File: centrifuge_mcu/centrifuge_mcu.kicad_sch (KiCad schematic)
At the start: 8 parts

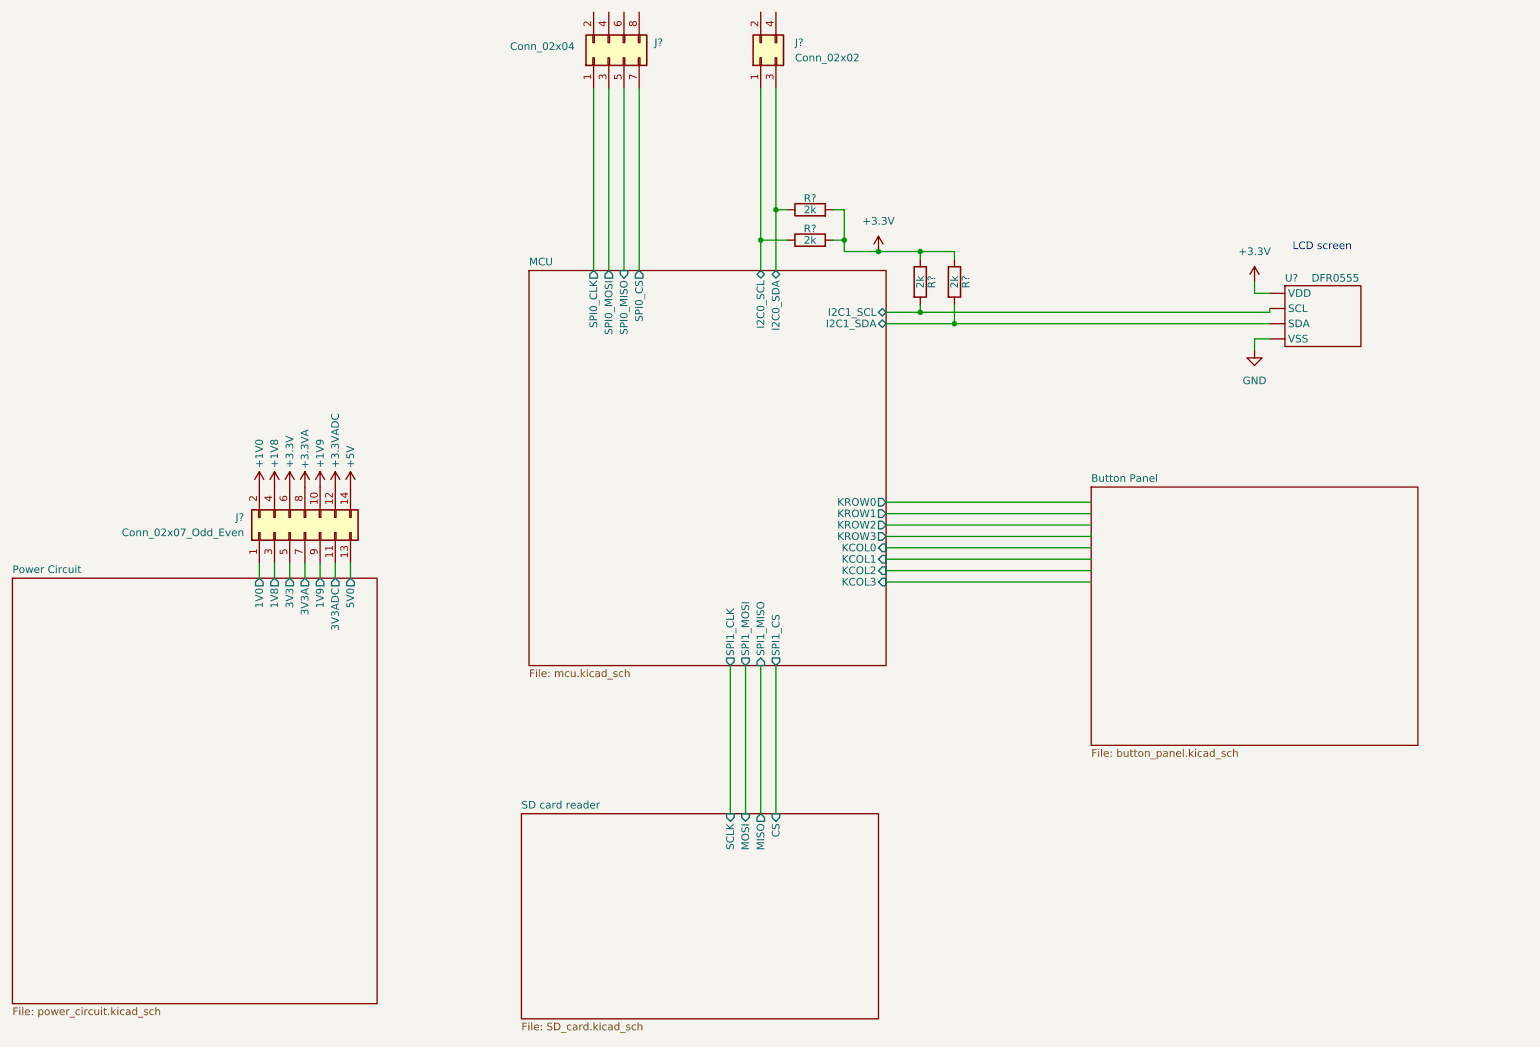
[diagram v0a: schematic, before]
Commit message: make and pick footprints for almost everything
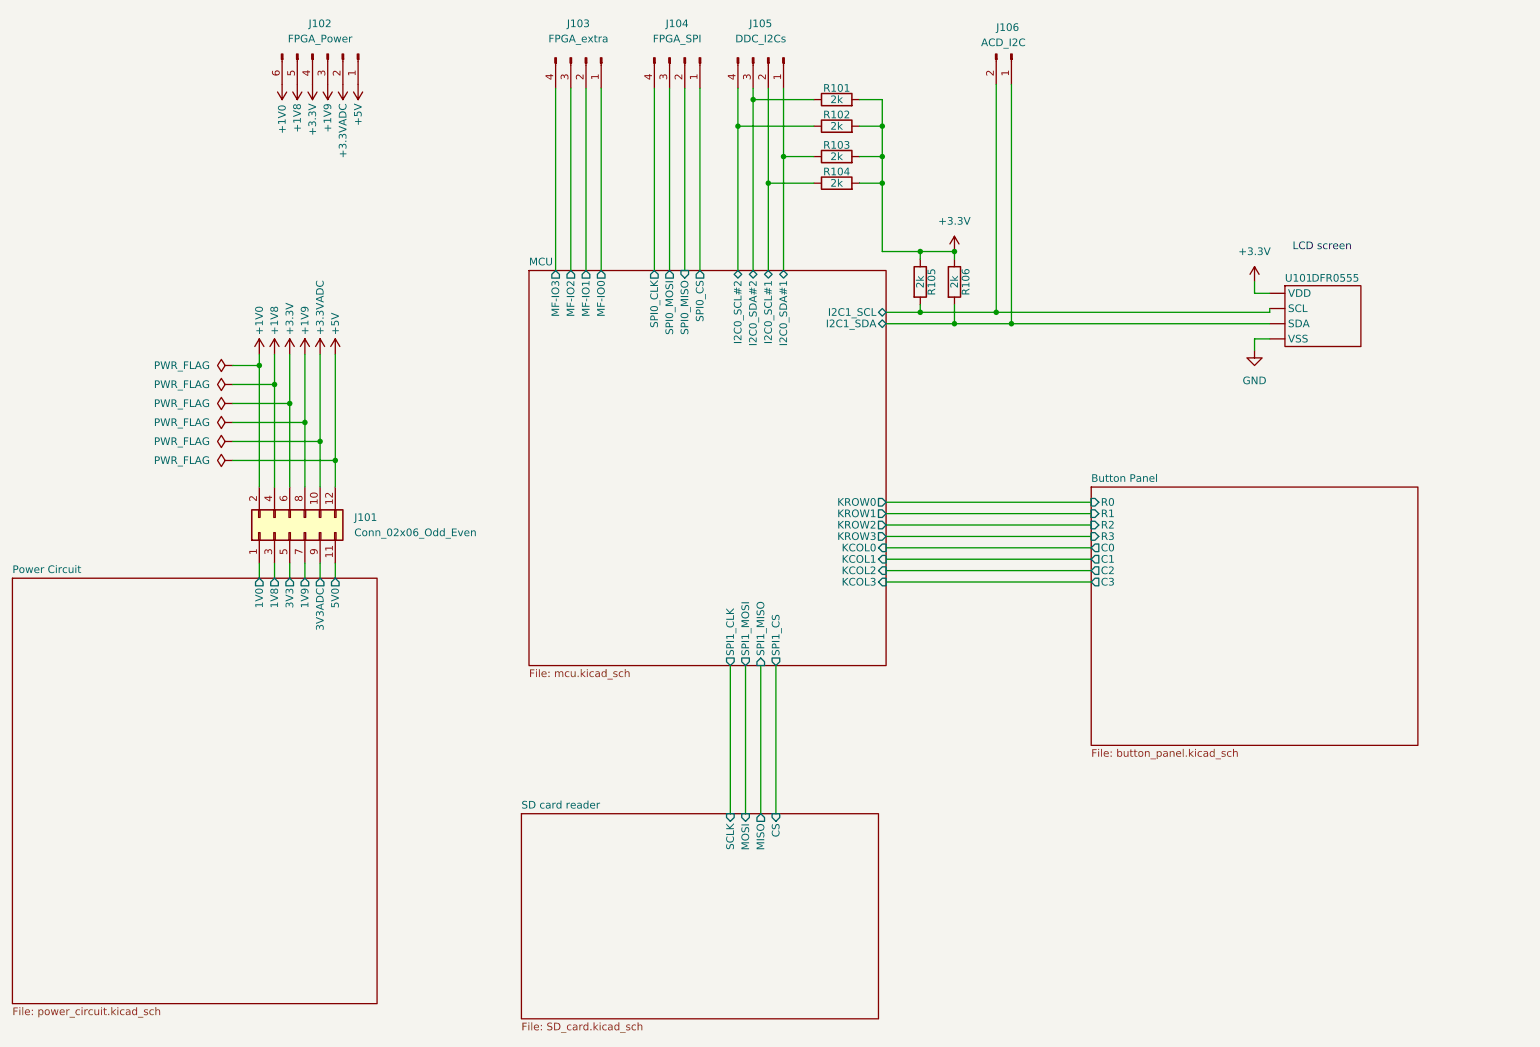
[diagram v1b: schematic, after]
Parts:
- removed J?: Conn_02x02, symbol Connector_Generic:Conn_02x02_Odd_Even
- removed J?: Conn_02x07_Odd_Even, symbol Connector_Generic:Conn_02x07_Odd_Even
- removed J?: Conn_02x04, symbol Connector_Generic:Conn_02x04_Odd_Even
- removed R? (x2): 2k, symbol Device:R
- added J101: Conn_02x06_Odd_Even, Connector_PinHeader_2.54mm:PinHeader_2x06_P2.54mm_Vertical, symbol Connector_Generic:Conn_02x06_Odd_Even
- added J102: FPGA_Power, Connector_PinHeader_2.54mm:PinHeader_1x06_P2.54mm_Vertical, symbol Connector:Conn_01x06_Male
- added J103: FPGA_extra, Connector_PinHeader_2.54mm:PinHeader_1x04_P2.54mm_Vertical, symbol Connector:Conn_01x04_Male
- added J104: FPGA_SPI, Connector_PinHeader_2.54mm:PinHeader_1x04_P2.54mm_Vertical, symbol Connector:Conn_01x04_Male
- added J105: DDC_I2Cs, Connector_PinHeader_2.54mm:PinHeader_1x04_P2.54mm_Vertical, symbol Connector:Conn_01x04_Male
- added J106: ACD_I2C, Connector_PinHeader_2.54mm:PinHeader_1x02_P2.54mm_Vertical, symbol Connector:Conn_01x02_Male
- added R101, R102, R103, R104: 2k, symbol Device:R
- gave numbers to parts that had none: 3
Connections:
- net +1V0: now also J101.2 (Pin_2), J102.6 (Pin_6)
- net +1V8: now also J101.4 (Pin_4), J102.5 (Pin_5)
- net +1V9: now also J101.8 (Pin_8), J102.3 (Pin_3)
- net +3.3V: now also J101.6 (Pin_6), J102.4 (Pin_4), R101.2, R102.2, R103.2, R104.2
- net +3.3VADC: now also J101.10 (Pin_10), J102.2 (Pin_2)
- net +5V: now also J101.12 (Pin_12), J102.1 (Pin_1)
- net MCU/I2C1_SCL: now also J106.2 (Pin_2)
- net MCU/I2C1_SDA: now also J106.1 (Pin_1)
- net MCU/SPI0_CLK: now also J104.4 (Pin_4)
- net MCU/SPI0_CS: now also J104.1 (Pin_1)
- net MCU/SPI0_MISO: now also J104.2 (Pin_2)
- net MCU/SPI0_MOSI: now also J104.3 (Pin_3)
- net Power Circuit/1V0: now also J101.1 (Pin_1)
- net Power Circuit/1V8: now also J101.3 (Pin_3)
- net Power Circuit/1V9: now also J101.7 (Pin_7)
- net Power Circuit/3V3: now also J101.5 (Pin_5)
- net Power Circuit/3V3ADC: now also J101.9 (Pin_9)
- net Power Circuit/5V0: now also J101.11 (Pin_11)
- new net MCU/I2C0_SCL#1: J105.2 (Pin_2), R104.1
- new net MCU/I2C0_SCL#2: J105.4 (Pin_4), R102.1
- new net MCU/I2C0_SDA#1: J105.1 (Pin_1), R103.1
- new net MCU/I2C0_SDA#2: J105.3 (Pin_3), R101.1
- new net MCU/MF-IO0: J103.1 (Pin_1)
- new net MCU/MF-IO1: J103.2 (Pin_2)
- new net MCU/MF-IO2: J103.3 (Pin_3)
- new net MCU/MF-IO3: J103.4 (Pin_4)
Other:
- sheet Button Panel ports: added C0, C1, C2, C3, R0, R1, R2, R3; removed none
- sheet MCU ports: added I2C0_SCL#1, I2C0_SCL#2, I2C0_SDA#1, I2C0_SDA#2, MF-IO0, MF-IO1, MF-IO2, MF-IO3; removed I2C0_SCL, I2C0_SDA
- sheet Power Circuit ports: added none; removed 3V3A

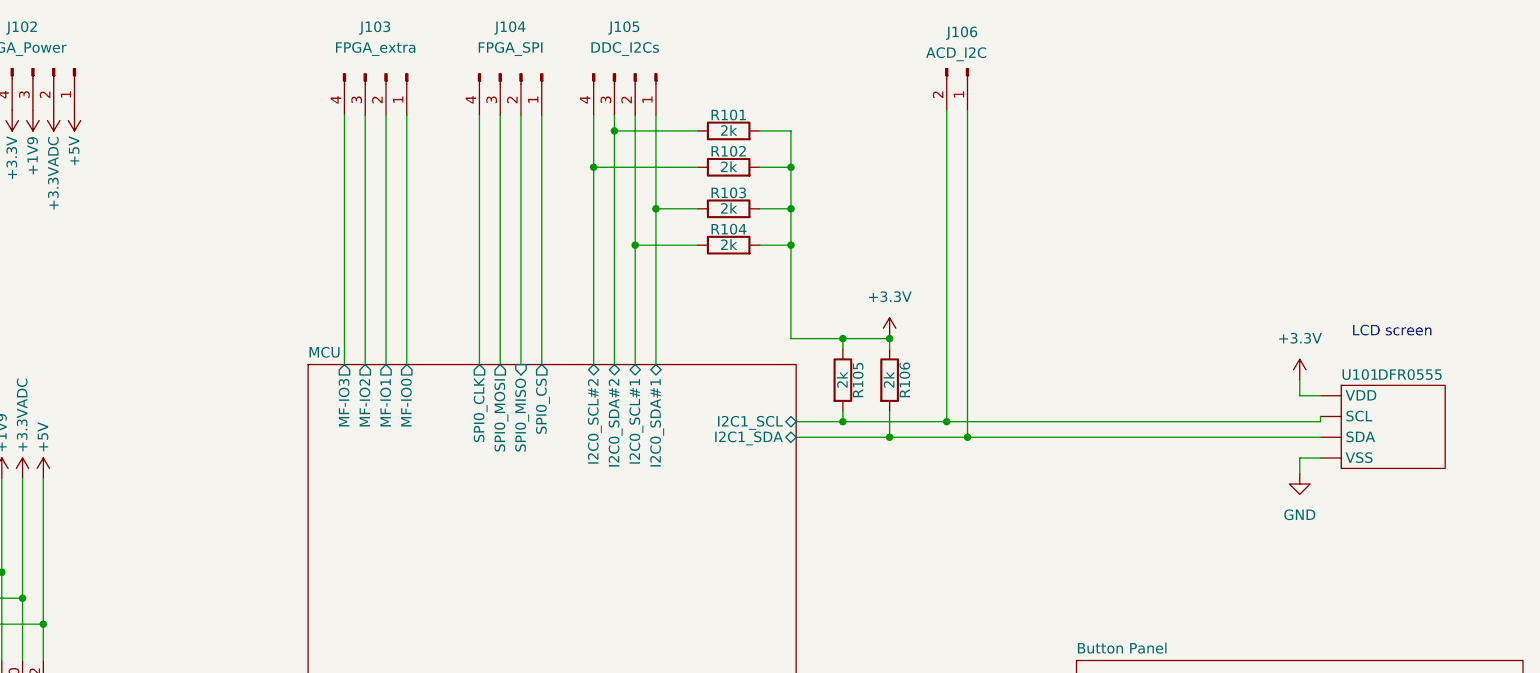
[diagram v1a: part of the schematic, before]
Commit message: more footprints, add links to resistor and inductance purchase
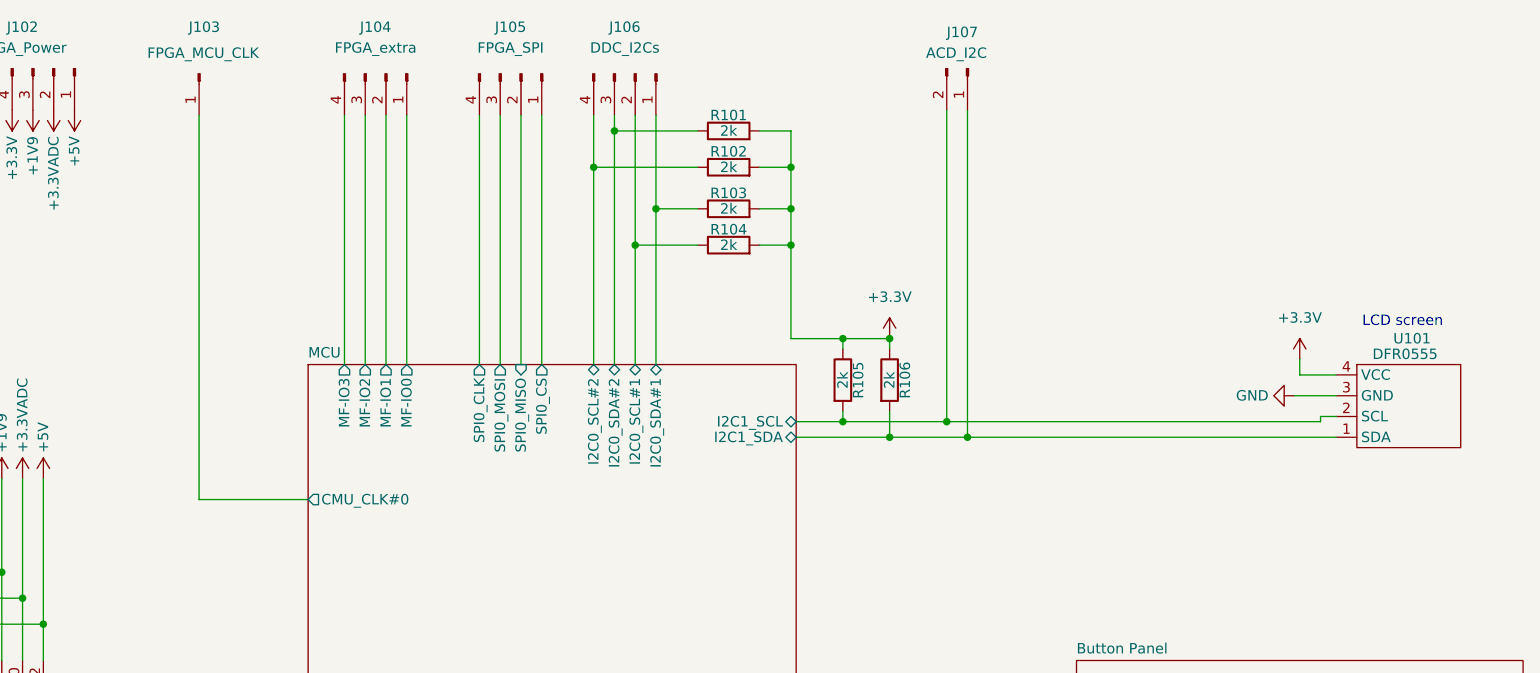
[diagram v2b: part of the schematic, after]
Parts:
- added J103: FPGA_MCU_CLK, Connector_PinHeader_2.54mm:PinHeader_1x01_P2.54mm_Vertical, symbol Connector:Conn_01x01_Male
- R101, R102, R103, R104, R105, R106: footprint (none) -> Resistor_SMD:R_0805_2012Metric_Pad1.20x1.40mm_HandSolder; Purchase (none) -> https://www.digikey.no/no/products/detail/yageo/AC0805FR-07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
- U101: footprint (none) -> centrifuge_mcu:DFR0555; Purchase (none) -> https://www.digikey.no/no/products/detail/trinamic-motion-c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
- renumbered J103 to J104, J104 to J105, J105 to J106, J106 to J107
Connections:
- net +3.3V: now also U101.4 (VCC); no longer U101. (VSS)
- net GND: now also U101.3 (GND); no longer U101. (VSS)
- net MCU/I2C1_SCL: now also U101.2 (SCL); no longer U101. (VSS)
- net MCU/I2C1_SDA: now also U101.1 (SDA); no longer U101. (VSS)
- new net MCU/CMU_CLK#0: J103.1 (Pin_1)
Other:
- sheet MCU ports: added CMU_CLK#0; removed none
- title: (none) -> VGA Centrifuge - MCU area

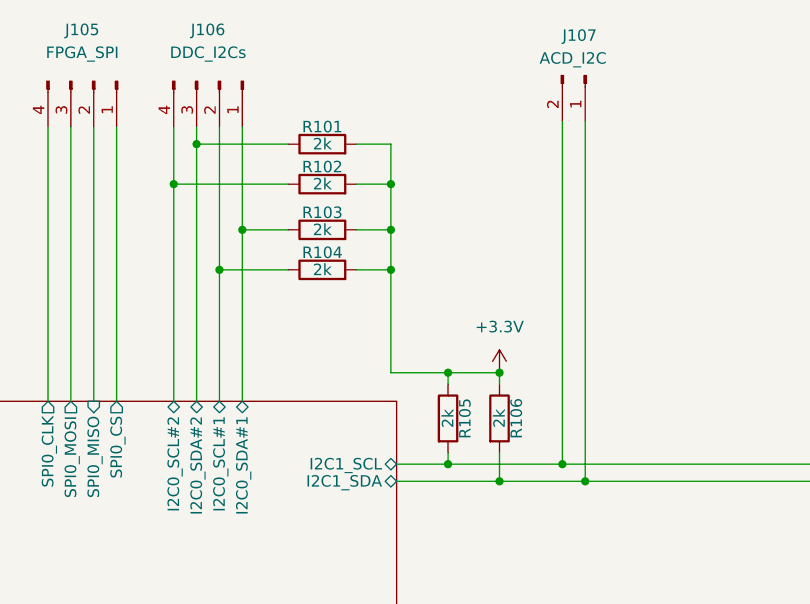
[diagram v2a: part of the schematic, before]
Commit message: last footprints, time to route (after final FPGA-board connectors)
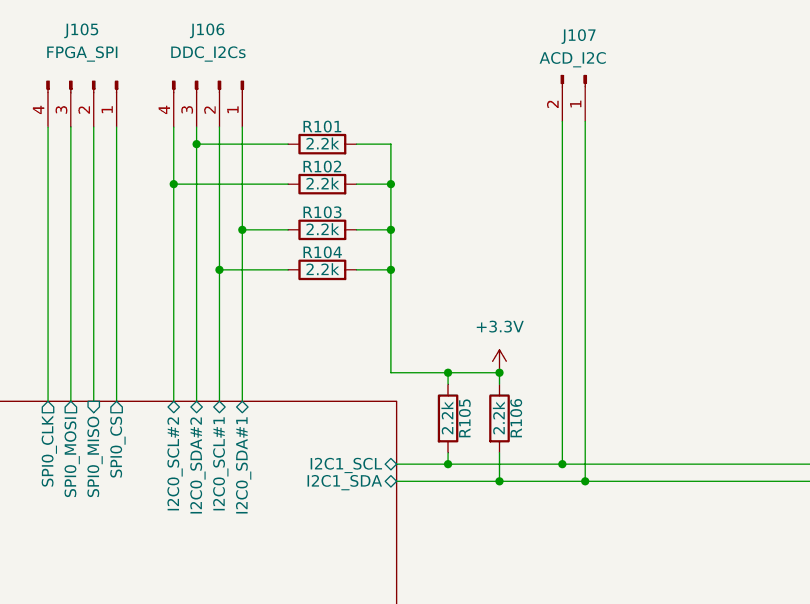
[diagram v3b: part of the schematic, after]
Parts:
- R101, R102, R103, R104, R105, R106: value 2k -> 2.2k; Purchase https://www.digikey.no/no/products/detail/yageo/AC0805FR-072KL/5896741 -> https://www.digikey.no/no/products/detail/yageo/AC0805FR-072K2L/5896727
- U101: footprint centrifuge_mcu:DFR0555 -> Connector_PinHeader_2.54mm:PinHeader_1x04_P2.54mm_Vertical

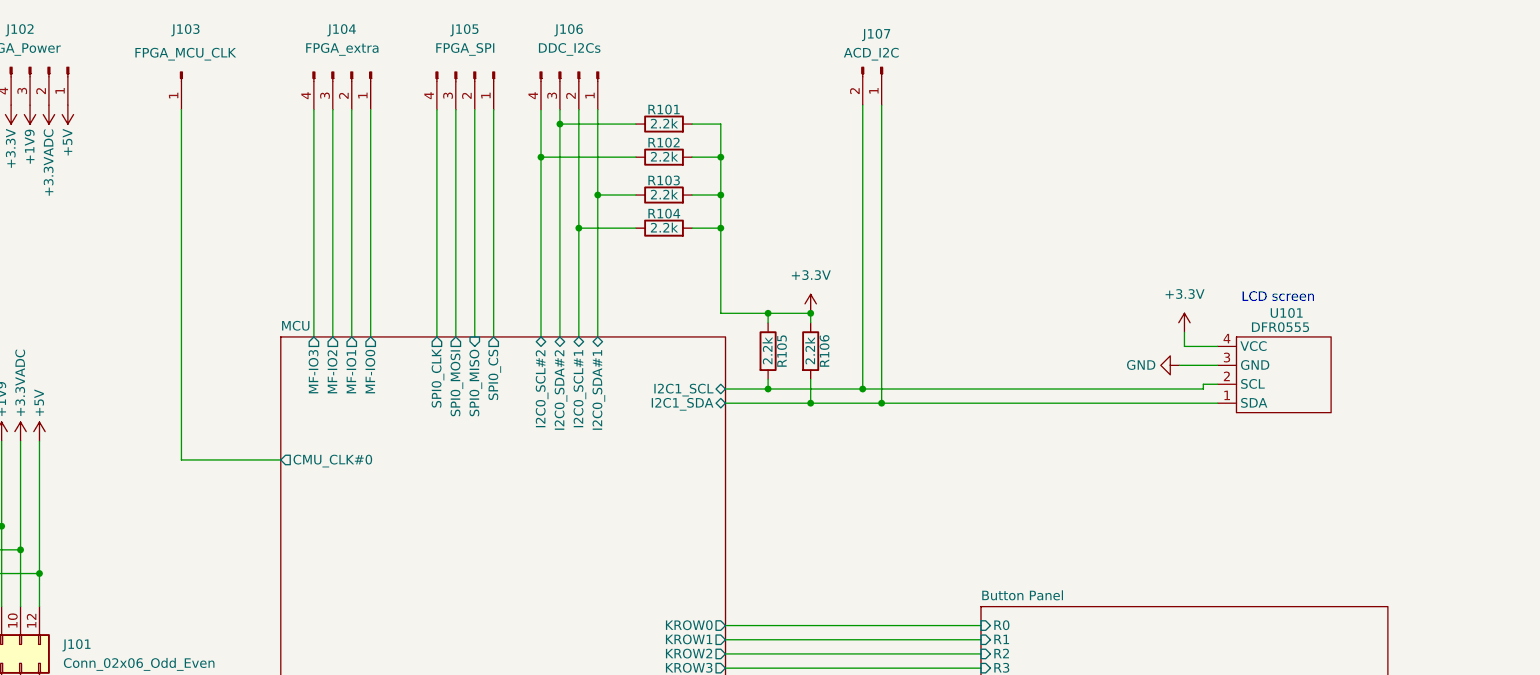
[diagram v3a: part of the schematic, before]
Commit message: start routing PCB for the MCU, starting with power
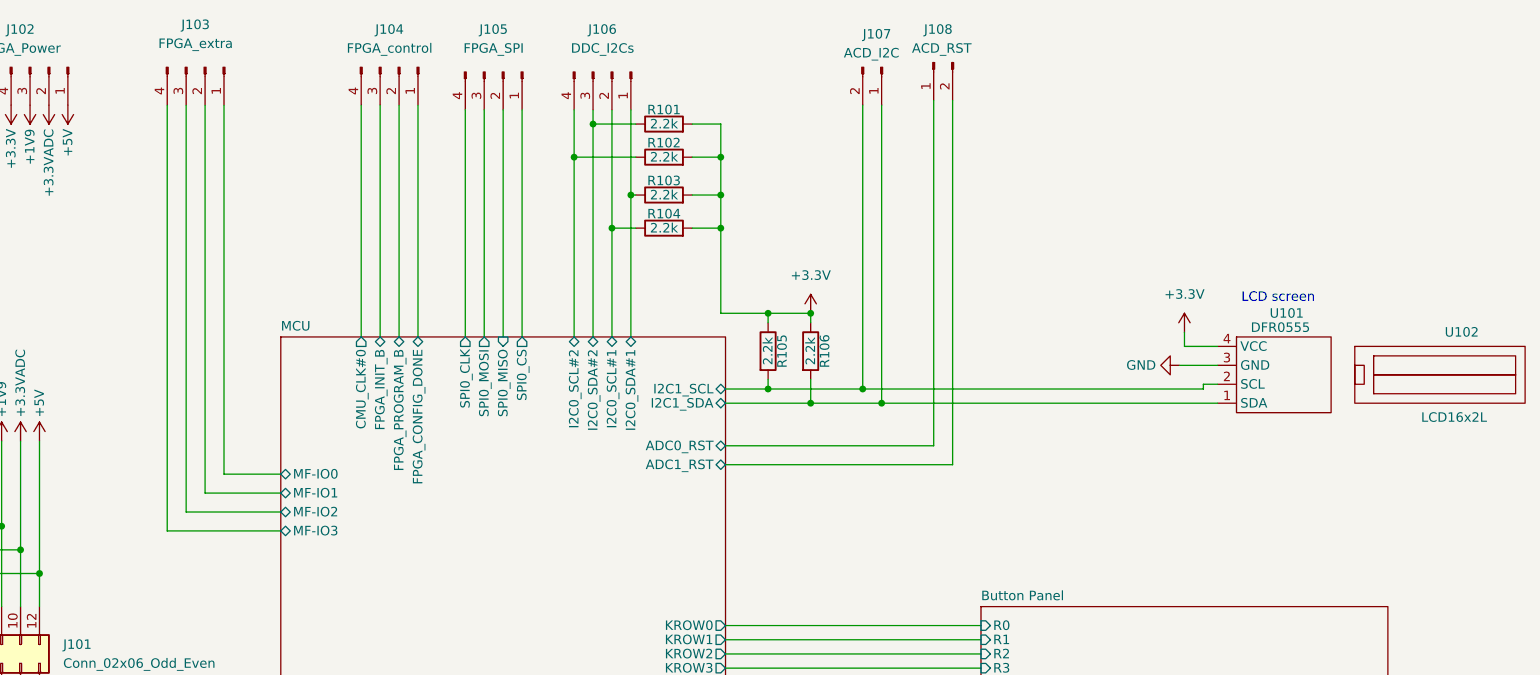
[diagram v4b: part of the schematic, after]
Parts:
- removed J103: FPGA_MCU_CLK, Connector_PinHeader_2.54mm:PinHeader_1x01_P2.54mm_Vertical, symbol Connector:Conn_01x01_Male
- added J104: FPGA_control, Connector_PinHeader_2.54mm:PinHeader_1x04_P2.54mm_Vertical, symbol Connector:Conn_01x04_Male
- added J108: ACD_RST, Connector_PinHeader_2.54mm:PinHeader_1x02_P2.54mm_Vertical, symbol Connector:Conn_01x02_Male
- added U102: LCD16x2L, centrifuge_mcu:DFR0555, symbol mcu_centrifuge_library:LCD16x2L
- renumbered J104 to J103
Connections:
- net MCU/CMU_CLK#0: now also J104.4 (Pin_4)
- new net MCU/ADC0_RST: J108.1 (Pin_1)
- new net MCU/ADC1_RST: J108.2 (Pin_2)
- new net MCU/FPGA_CONFIG_DONE: J104.1 (Pin_1)
- new net MCU/FPGA_INIT_B: J104.3 (Pin_3)
- new net MCU/FPGA_PROGRAM_B: J104.2 (Pin_2)
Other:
- sheet MCU ports: added ADC0_RST, ADC1_RST, FPGA_CONFIG_DONE, FPGA_INIT_B, FPGA_PROGRAM_B; removed none
- moved on the sheet: J103, J105, J106
